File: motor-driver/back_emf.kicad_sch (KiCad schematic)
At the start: 6 parts, among them U15 LM397

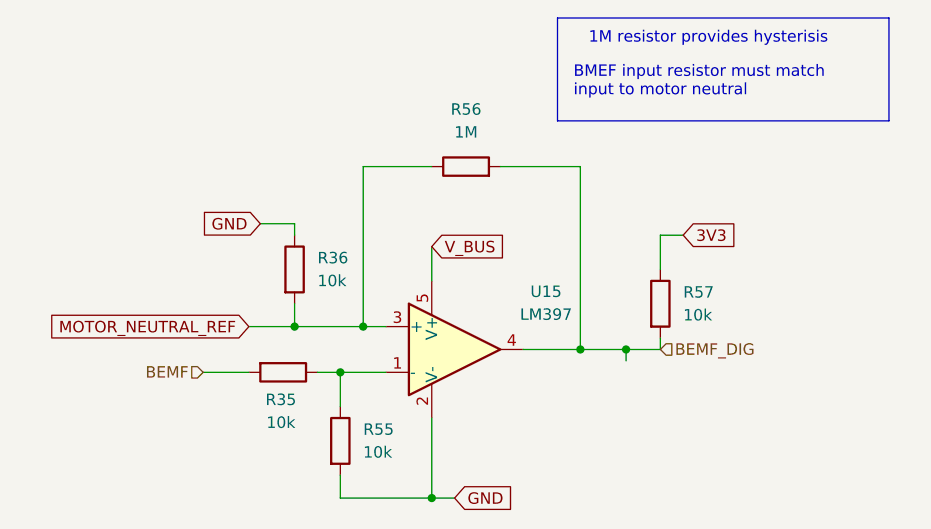
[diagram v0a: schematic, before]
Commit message: added spi connection
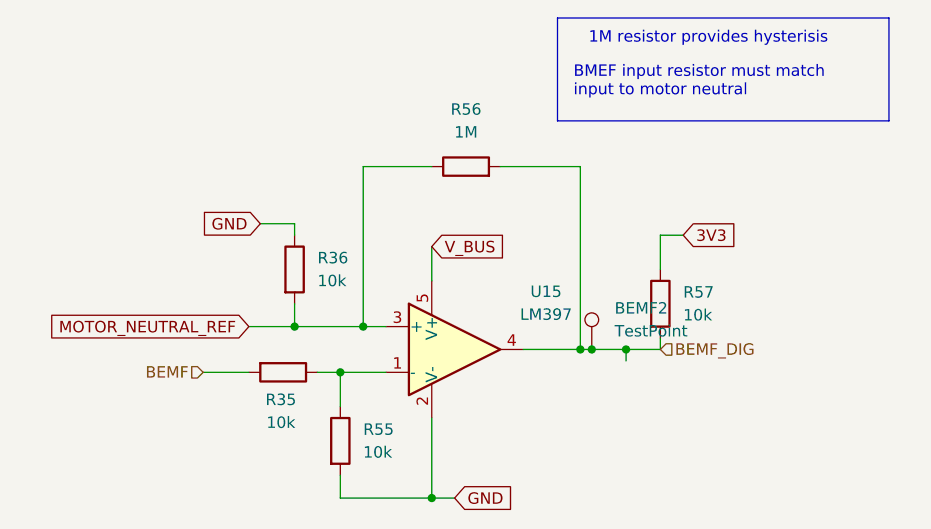
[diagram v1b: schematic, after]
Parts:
- added BEMF2: TestPoint, TestPoint:TestPoint_Loop_D1.80mm_Drill1.0mm_Beaded, symbol Connector:TestPoint
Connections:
- net BEMF_DIG: now also BEMF2.1
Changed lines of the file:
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@@
+	)
+	(junction
+		(at 160.02 100.33)
+		(diameter 0)
+		(color 0 0 0 0)
 	)
 	(junction
@@
 	(wire
 		(pts
+			(xy 160.02 100.33) (xy 163.83 100.33)
+		)
+		(stroke
+			(width 0)
+			(type default)
+		)
+	)
+	(wire
+		(pts
 			(xy 142.24 88.9) (xy 142.24 92.71)
 		)
@@
 	(wire
 		(pts
-			(xy 158.75 100.33) (xy 163.83 100.33)
+			(xy 158.75 100.33) (xy 160.02 100.33)
 		)
 		(stroke
@@
 					(unit 1)
 				)
+			)
+		)
+	)
+	(symbol
+		(lib_id "Connector:TestPoint")
+		(at 160.02 100.33 0)
+		(unit 1)
+		(exclude_from_sim no)
+		(in_bom no)
+		(on_board yes)
+		(dnp no)
+		(fields_autoplaced yes)
+		(property "Reference" "BEMF2"
+			(at 162.56 95.7579 0)
+			(effects
+				(font
+					(size 1.27 1.27)
+				)
+				(justify left)
+			)
+		)
+		(property "Value" "TestPoint"
+			(at 162.56 98.2979 0)
+			(effects
+				(font
+					(size 1.27 1.27)
+				)
+				(justify left)
+			)
+		)
+		(property "Footprint" "TestPoint:TestPoint_Loop_D1.80mm_Drill1.0mm_Beaded"
+			(at 165.1 100.33 0)
+			(effects
+				(font
+					(size 1.27 1.27)
+				)
+				(hide yes)
+			)
+		)
+		(property "Datasheet" "~"
+			(at 165.1 100.33 0)
+			(effects
+				(font
+					(size 1.27 1.27)
+				)
+				(hide yes)
+			)
+		)
+		(property "Description" "test point"
+			(at 160.02 100.33 0)
+			(effects
+				(font
+					(size 1.27 1.27)
+				)
+				(hide yes)
+			)
+		)
+		(pin "1"
+		)
+		(instances
+			(project "motor-driver"
+				(path "/2980fc7e-b297-4843-ba9f-cceafa384b2f/d36b7053-ee22-4492-bdec-8a6a56460e2b/5dcb47c1-5cbd-4c06-ae20-6bf4ebc0293f"
+					(reference "BMEF1")
+					(unit 1)
+				)
+				(path "/2980fc7e-b297-4843-ba9f-cceafa384b2f/d36b7053-ee22-4492-bdec-8a6a56460e2b/d55dfac5-5848-47fb-8309-2ae121a74f55"
+					(reference "BEMF3")
+					(unit 1)
+				)
+				(path "/2980fc7e-b297-4843-ba9f-cceafa384b2f/d36b7053-ee22-4492-bdec-8a6a56460e2b/e5439fff-5f30-49ba-87ec-c8b9c8d18afa"
+					(reference "BEMF2")
+					(unit 1)
+				)

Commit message: added test points
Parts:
- removed BEMF2: TestPoint, TestPoint:TestPoint_Loop_D1.80mm_Drill1.0mm_Beaded, symbol Connector:TestPoint
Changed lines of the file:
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@@
-	)
-	(junction
-		(at 160.02 100.33)
-		(diameter 0)
-		(color 0 0 0 0)
 	)
 	(junction
@@
 	(wire
 		(pts
-			(xy 160.02 100.33) (xy 163.83 100.33)
-		)
-		(stroke
-			(width 0)
-			(type default)
-		)
-	)
-	(wire
-		(pts
 			(xy 142.24 88.9) (xy 142.24 92.71)
 		)
@@
 	(wire
 		(pts
-			(xy 158.75 100.33) (xy 160.02 100.33)
+			(xy 158.75 100.33) (xy 163.83 100.33)
 		)
 		(stroke
@@
 					(unit 1)
 				)
-			)
-		)
-	)
-	(symbol
-		(lib_id "Connector:TestPoint")
-		(at 160.02 100.33 0)
-		(unit 1)
-		(exclude_from_sim no)
-		(in_bom no)
-		(on_board yes)
-		(dnp no)
-		(fields_autoplaced yes)
-		(property "Reference" "BEMF2"
-			(at 162.56 95.7579 0)
-			(effects
-				(font
-					(size 1.27 1.27)
-				)
-				(justify left)
-			)
-		)
-		(property "Value" "TestPoint"
-			(at 162.56 98.2979 0)
-			(effects
-				(font
-					(size 1.27 1.27)
-				)
-				(justify left)
-			)
-		)
-		(property "Footprint" "TestPoint:TestPoint_Loop_D1.80mm_Drill1.0mm_Beaded"
-			(at 165.1 100.33 0)
-			(effects
-				(font
-					(size 1.27 1.27)
-				)
-				(hide yes)
-			)
-		)
-		(property "Datasheet" "~"
-			(at 165.1 100.33 0)
-			(effects
-				(font
-					(size 1.27 1.27)
-				)
-				(hide yes)
-			)
-		)
-		(property "Description" "test point"
-			(at 160.02 100.33 0)
-			(effects
-				(font
-					(size 1.27 1.27)
-				)
-				(hide yes)
-			)
-		)
-		(pin "1"
-		)
-		(instances
-			(project "motor-driver"
-				(path "/2980fc7e-b297-4843-ba9f-cceafa384b2f/d36b7053-ee22-4492-bdec-8a6a56460e2b/5dcb47c1-5cbd-4c06-ae20-6bf4ebc0293f"
-					(reference "BMEF1")
-					(unit 1)
-				)
-				(path "/2980fc7e-b297-4843-ba9f-cceafa384b2f/d36b7053-ee22-4492-bdec-8a6a56460e2b/d55dfac5-5848-47fb-8309-2ae121a74f55"
-					(reference "BEMF3")
-					(unit 1)
-				)
-				(path "/2980fc7e-b297-4843-ba9f-cceafa384b2f/d36b7053-ee22-4492-bdec-8a6a56460e2b/e5439fff-5f30-49ba-87ec-c8b9c8d18afa"
-					(reference "BEMF2")
-					(unit 1)
-				)
